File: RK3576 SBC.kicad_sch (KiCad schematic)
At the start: 0 parts

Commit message: Add files via upload
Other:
- added sheet Mechanical (mechanical.kicad_sch)
- added sheet RTC (rtc.kicad_sch)
- sheet 4x USB Hub ports: added USB3_HOST1, USB3_HOST2, USB3_HOST3, USB3_HOST4, USB3_OTG1_USB_HUB; removed USB_{HOST1}_Data, USB_{HOST2}_Data, USB_{HOST3}_Data, USB_{HOST4}_Data, USB_{HUB}_Data
- sheet Ethernet ports: added RGMII_RX, RGMII_TX; removed PHY_CLK_{OUT}, RGMII
- sheet HDMI ports: added HDMI, HDMI_GPIOs, HDMI_PWREN_H; removed HDMI_CTRL, HDMI_DATA, I2C
- sheet MIPI ports: added MIPI_CSI12, MIPI_CSI_CTRL, MIPI_DSI0; removed CSI_CTRL, CSI_DATA, DSI_CTRL, DSI_DATA, I2C
- sheet PCIe ports: added PCIE0, PCIE0_CTRL; removed PCIe_CTRL, PCIe_DATA
- sheet USB3.2 Host ports: added USB3_HOST1, USB3_HOST2, USB3_HOST3, USB3_HOST4, USB3_HOST_PWREN_H; removed USB_{HOST1}_Data, USB_{HOST2}_Data, USB_{HOST3}_Data, USB_{HOST4}_Data, USB_{HOST}_PWR_EN
- sheet USB3.2 OTG ports: added USB_C_OTG0, USB_C_OTG0_GPIOs; removed I2C, USB_{OTG}_AUX, USB_{OTG}_CON_INT, USB_{OTG}_Data
- sheet WIFI & Blutooth ports: added BT_BCM, BT_GPIOs, RTC_32KOUT_WIFI, WIFI_BT_ANT_CTRL, WIFI_GPIOs; removed BT_PCM
- sheet uSD Card ports: added uSD_CARD, uSD_PWREN_H; removed uSD_SDIO
- note added: "OPEN SOURCE HARDWARE"

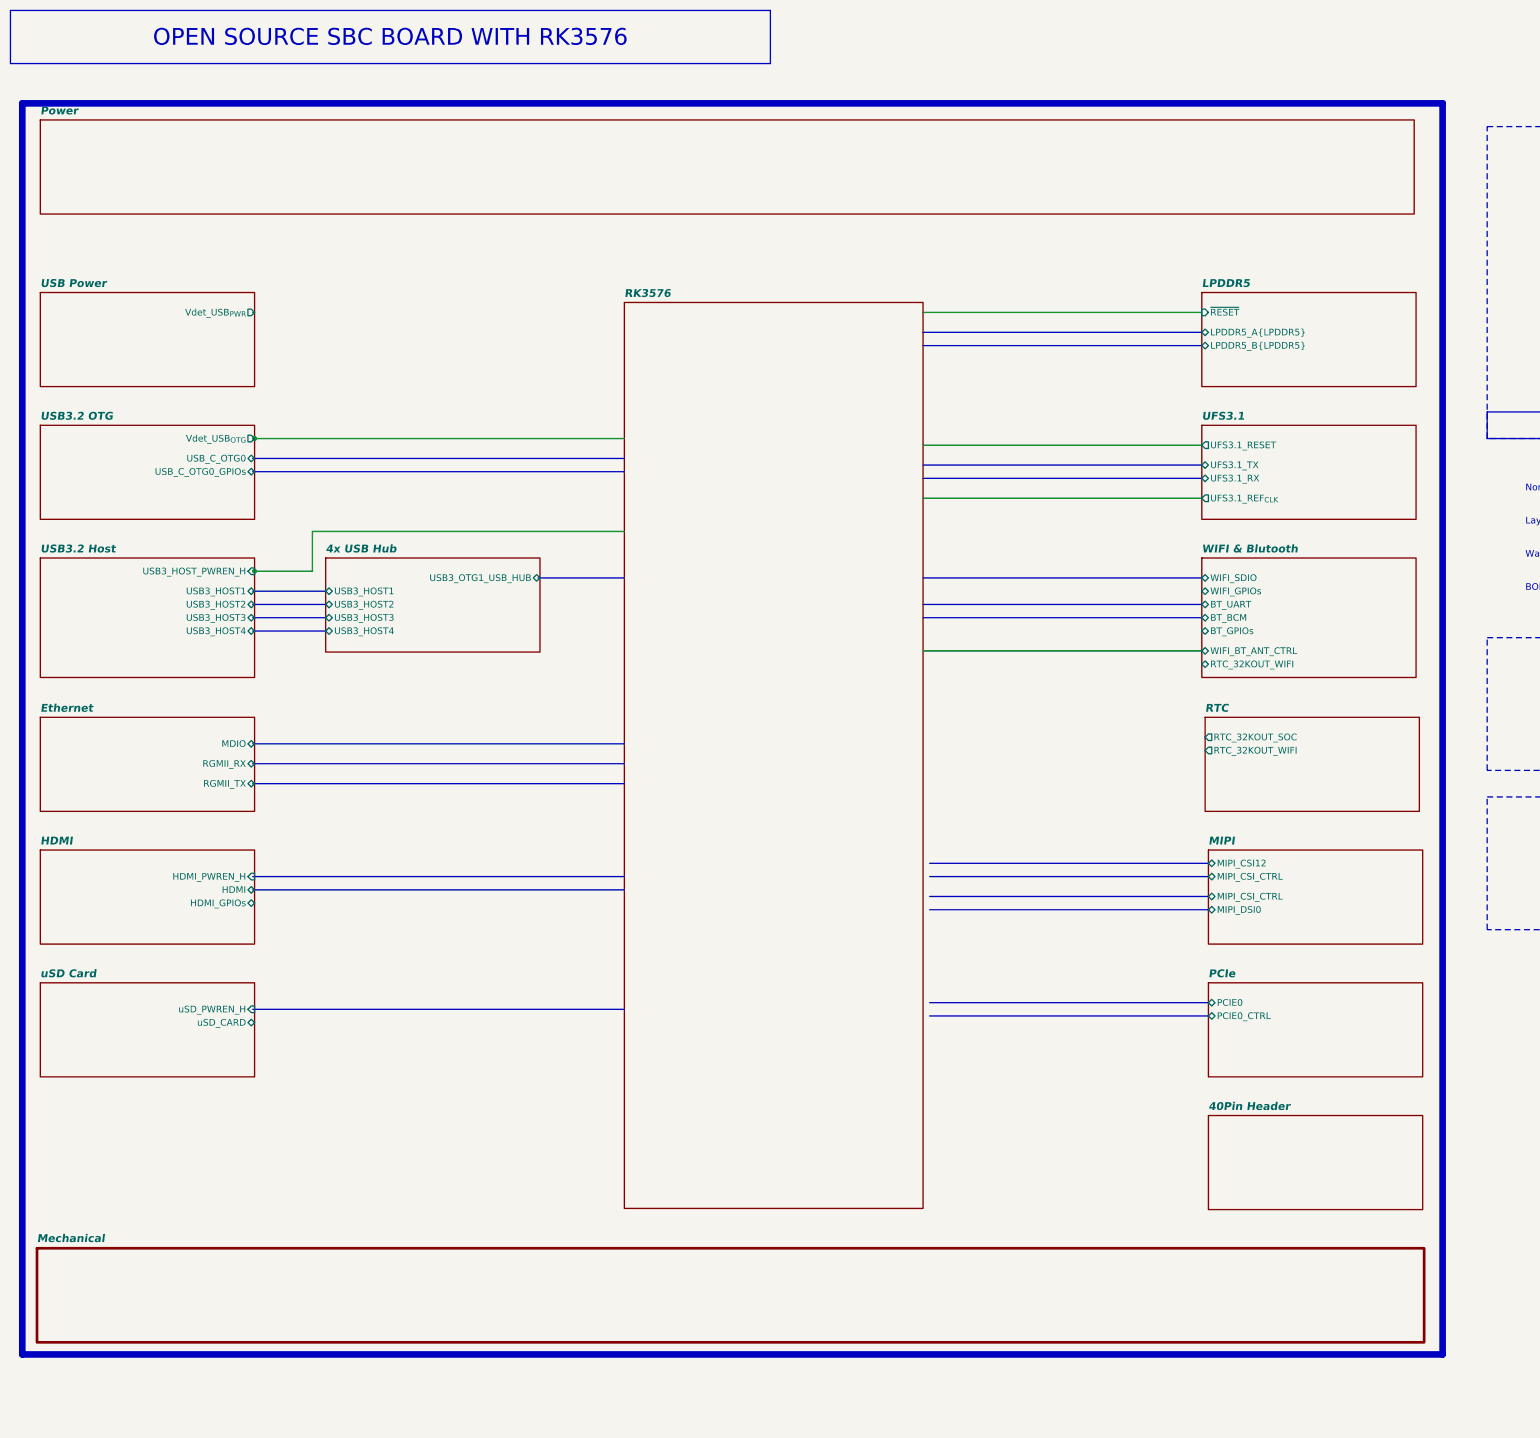
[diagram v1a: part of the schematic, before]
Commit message: SBC Board V0.2
The SBC schematics before footprint and part number check
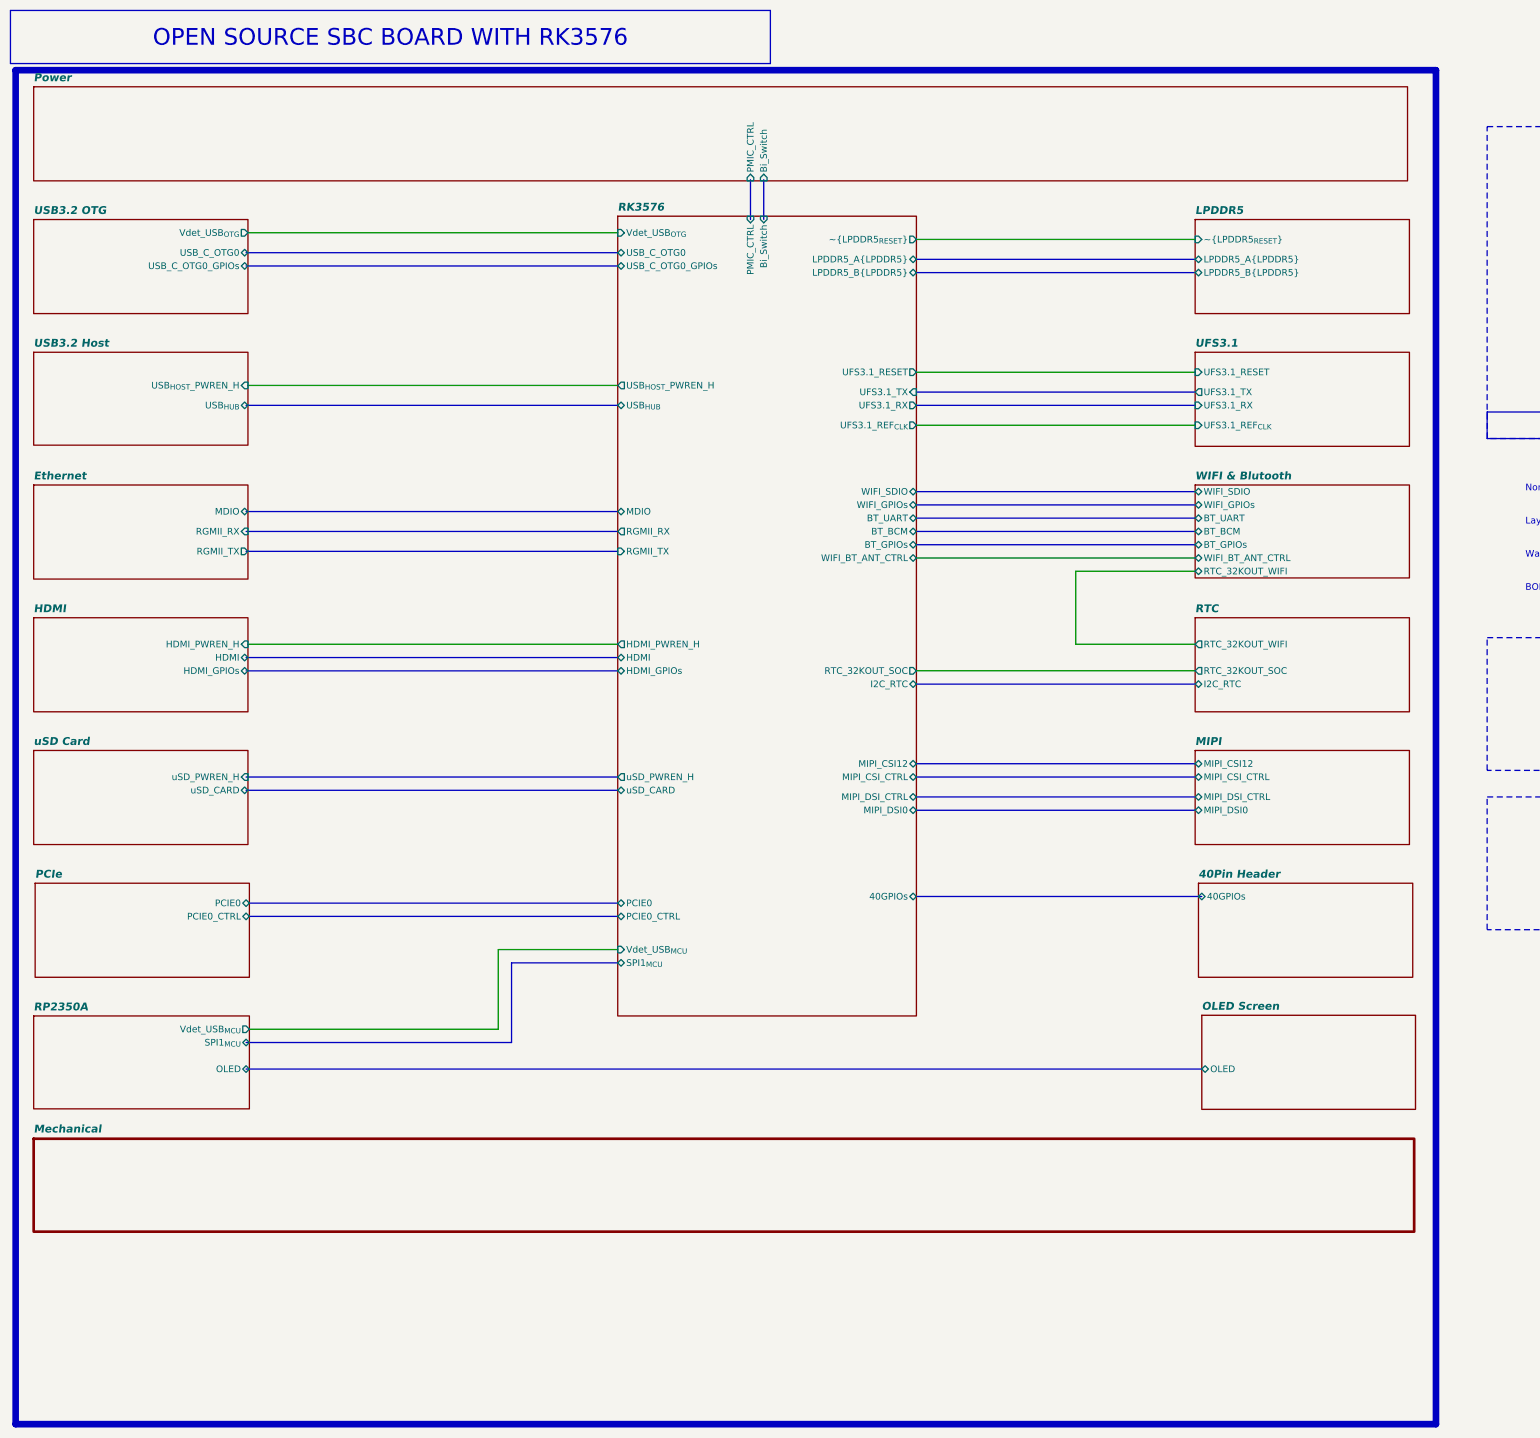
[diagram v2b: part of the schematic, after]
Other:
- removed sheet 4x USB Hub
- removed sheet USB Power
- added sheet OLED Screen (oled_screen.kicad_sch)
- added sheet RP2350A (RP2350A.kicad_sch)
- sheet 40Pin Header ports: added 40GPIOs; removed none
- sheet LPDDR5 ports: added ~{LPDDR5_{RESET}}; removed ~{RESET}
- sheet MIPI ports: added MIPI_DSI_CTRL; removed none
- sheet Power ports: added Bi_Switch, PMIC_CTRL; removed none
- sheet RK3576 ports: added 40GPIOs, BT_BCM, BT_GPIOs, BT_UART, Bi_Switch, HDMI, HDMI_GPIOs, HDMI_PWREN_H, I2C_RTC, LPDDR5_A{LPDDR5}, LPDDR5_B{LPDDR5}, MDIO, MIPI_CSI12, MIPI_CSI_CTRL, MIPI_DSI0, MIPI_DSI_CTRL, PCIE0, PCIE0_CTRL, PMIC_CTRL, RGMII_RX, RGMII_TX, RTC_32KOUT_SOC, SPI1_{MCU}, UFS3.1_REF_{CLK}, UFS3.1_RESET, UFS3.1_RX, UFS3.1_TX, USB_C_OTG0, USB_C_OTG0_GPIOs, USB_{HOST}_PWREN_H, USB_{HUB}, Vdet_USB_{MCU}, Vdet_USB_{OTG}, WIFI_BT_ANT_CTRL, WIFI_GPIOs, WIFI_SDIO, uSD_CARD, uSD_PWREN_H, ~{LPDDR5_{RESET}}; removed none
- sheet RTC ports: added I2C_RTC; removed none
- sheet USB3.2 Host ports: added USB_{HOST}_PWREN_H, USB_{HUB}; removed USB3_HOST1, USB3_HOST2, USB3_HOST3, USB3_HOST4, USB3_HOST_PWREN_H

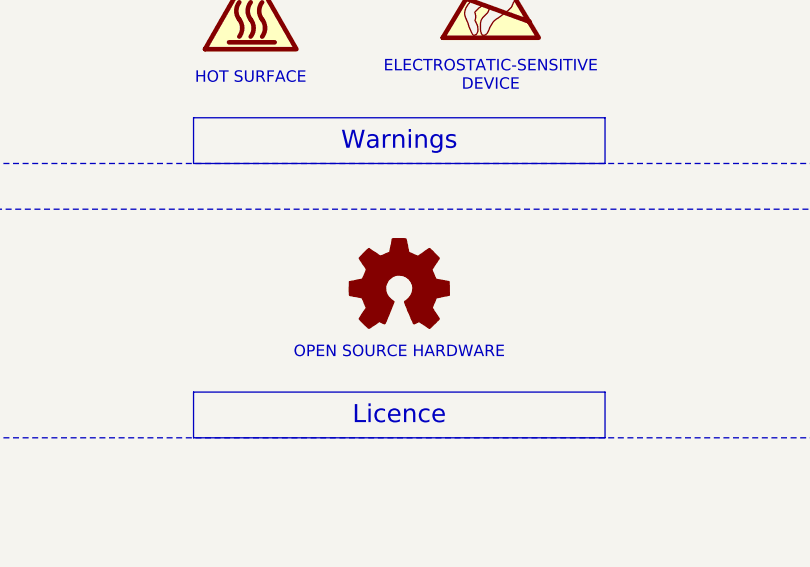
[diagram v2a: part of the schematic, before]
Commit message: SBCv0.3
there is no big thing update just some LCSC & Mouser parts
and Big problem deleted alot of component values (:
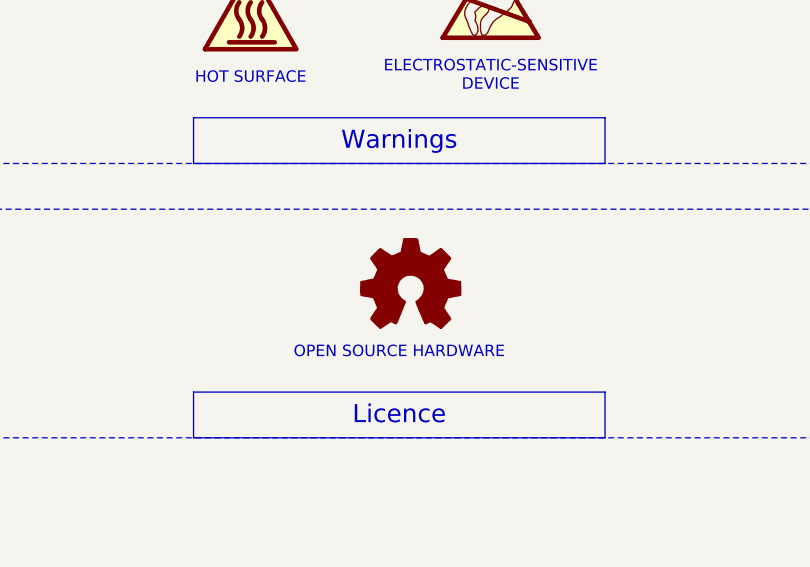
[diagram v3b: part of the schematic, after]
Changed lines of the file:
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@@
-	)
-	(symbol
-		(lib_id "Graphic:Logo_Open_Hardware_Small")
-		(at 347.98 171.45 0)
-		(unit 1)
-		(body_style 1)
-		(exclude_from_sim yes)
-		(in_bom no)
-		(on_board no)
-		(in_pos_files yes)
-		(dnp no)
-		(fields_autoplaced yes)
-		(property "Reference" "#SYM2"
-			(at 347.98 164.465 0)
-			(hide yes)
-			(show_name no)
-			(do_not_autoplace no)
-			(effects
-				(font
-					(size 1.27 1.27)
-				)
-			)
-		)
-		(property "Value" "Logo_Open_Hardware_Small"
-			(at 347.98 177.165 0)
-			(hide yes)
-			(show_name no)
-			(do_not_autoplace no)
-			(effects
-				(font
-					(size 1.27 1.27)
-				)
-			)
-		)
-		(property "Footprint" ""
-			(at 347.98 171.45 0)
-			(hide yes)
-			(show_name no)
-			(do_not_autoplace no)
-			(effects
-				(font
-					(size 1.27 1.27)
-				)
-			)
-		)
-		(property "Datasheet" ""
-			(at 347.98 171.45 0)
-			(hide yes)
-			(show_name no)
-			(do_not_autoplace no)
-			(effects
-				(font
-					(size 1.27 1.27)
-				)
-			)
-		)
-		(property "Description" "Open Hardware logo, small"
-			(at 347.98 171.45 0)
-			(hide yes)
-			(show_name no)
-			(do_not_autoplace no)
-			(effects
-				(font
-					(size 1.27 1.27)
-				)
-			)
-		)
-		(instances
-			(project "RK3576 SBC"
-				(path "/b79dbff4-0cad-4ff7-bec2-7c0e4f8b14d3"
-					(reference "#SYM2")
-					(unit 1)
-				)
-			)
-		)
 	)
 	(symbol
@@
 					(unit 1)
 				)
+			)
+		)
+	)
+	(symbol
+		(lib_id "Graphic:Logo_Open_Hardware_Small")
+		(at 349.25 171.45 0)
+		(unit 1)
+		(body_style 1)
+		(exclude_from_sim yes)
+		(in_bom no)
+		(on_board no)
+		(in_pos_files yes)
+		(dnp no)
+		(fields_autoplaced yes)
+		(property "Reference" "#SYM3"
+			(at 349.25 164.465 0)
+			(hide yes)
+			(show_name no)
+			(do_not_autoplace no)
+			(effects
+				(font
+					(size 1.27 1.27)
+				)
+			)
+		)
+		(property "Value" "Logo_Open_Hardware_Small"
+			(at 349.25 177.165 0)
+			(hide yes)
+			(show_name no)
+			(do_not_autoplace no)
+			(effects
+				(font
+					(size 1.27 1.27)
+				)
+			)
+		)
+		(property "Footprint" ""
+			(at 349.25 171.45 0)
+			(hide yes)
+			(show_name no)
+			(do_not_autoplace no)
+			(effects
+				(font
+					(size 1.27 1.27)
+				)
+			)
+		)
+		(property "Datasheet" ""
+			(at 349.25 171.45 0)
+			(hide yes)
+			(show_name no)
+			(do_not_autoplace no)
+			(effects
+				(font
+					(size 1.27 1.27)
+				)
+			)
+		)
+		(property "Description" "Open Hardware logo, small"
+			(at 349.25 171.45 0)
+			(hide yes)
+			(show_name no)
+			(do_not_autoplace no)
+			(effects
+				(font
+					(size 1.27 1.27)
+				)
+			)
+		)
+		(instances
+			(project "RK3576 SBC"
+				(path "/b79dbff4-0cad-4ff7-bec2-7c0e4f8b14d3"
+					(reference "#SYM3")
+					(unit 1)
+				)
